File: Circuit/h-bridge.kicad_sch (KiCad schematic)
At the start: 8 parts, among them Q1 PNP, Q2 NPN, Q3 PNP, Q4 NPN

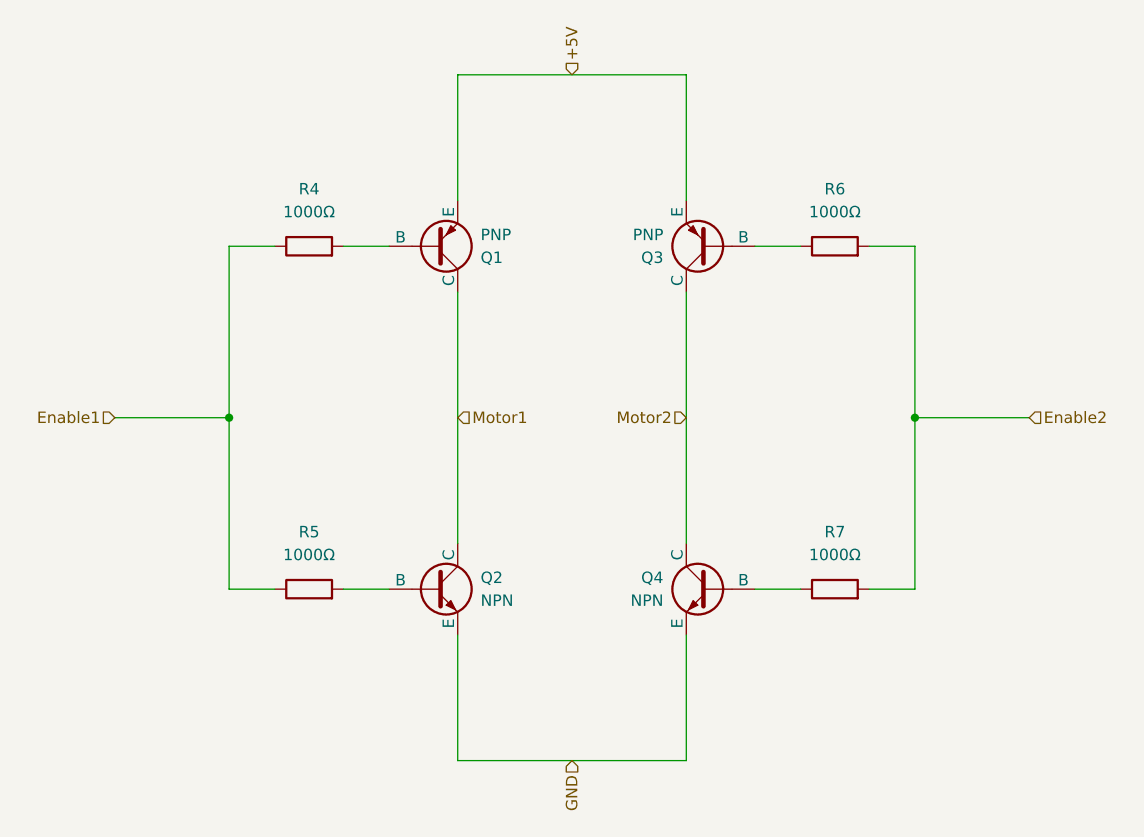
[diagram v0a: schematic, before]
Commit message: Added support for 2 power supplies (5V and 0-30V) and used mosfets
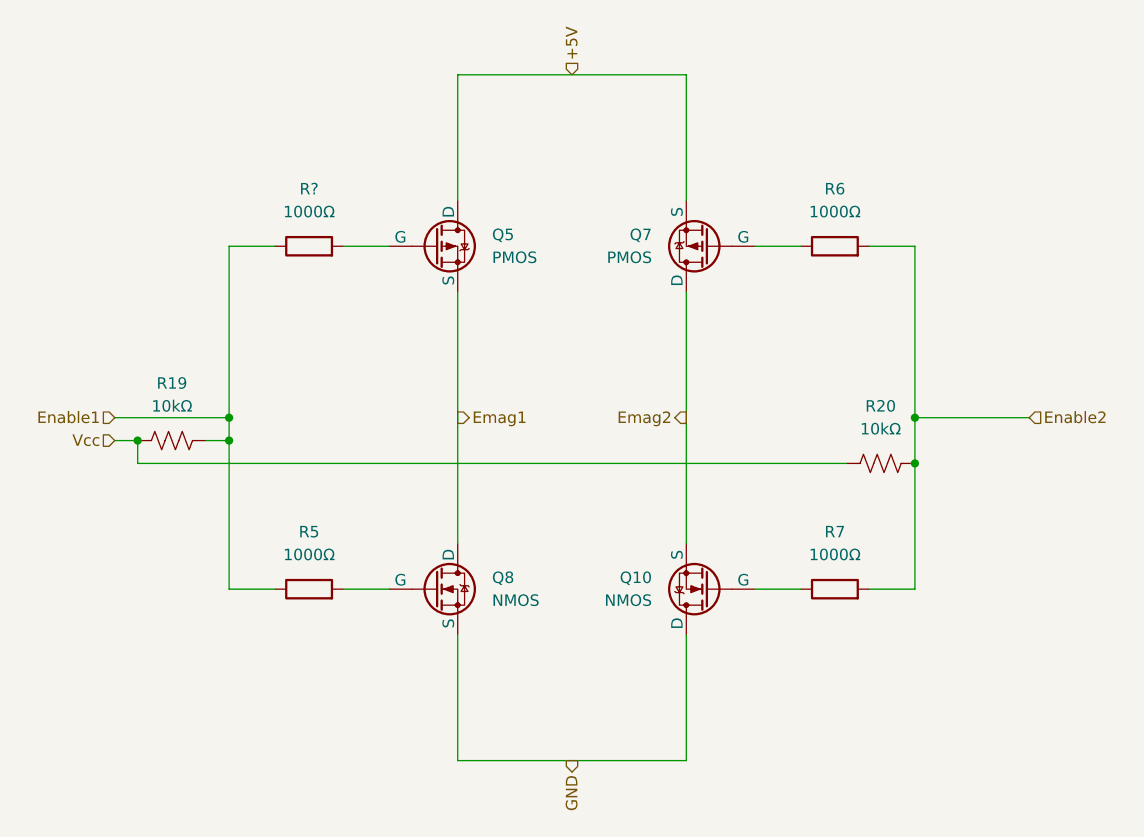
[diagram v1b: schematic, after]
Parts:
- removed Q1, Q3: PNP, symbol Simulation_SPICE:PNP
- removed Q2, Q4: NPN, symbol Simulation_SPICE:NPN
- added Q10, Q8: NMOS, symbol Simulation_SPICE:NMOS
- added Q5, Q7: PMOS, symbol Simulation_SPICE:PMOS
- added R19, R20: 10kΩ, symbol Device:R_US
- renumbered R4 to R?
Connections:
- net +5V: now also Q5.1 (D), Q7.3 (S)
- net Enable1: now also R19.2
- net Enable2: now also R20.2
- net GND: now also Q10.1 (D), Q8.3 (S)
- net at R6.1: now also Q7.2 (G)
- net at R5.2: now also Q8.2 (G)
- net at R?.2: now also Q5.2 (G)
- net at R7.1: now also Q10.2 (G)
- new net Emag1: Q5.3 (S), Q8.1 (D)
- new net Emag2: Q10.3 (S), Q7.1 (D)
- new net Vcc: R19.1, R20.1
